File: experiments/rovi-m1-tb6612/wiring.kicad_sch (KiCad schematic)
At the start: 0 parts

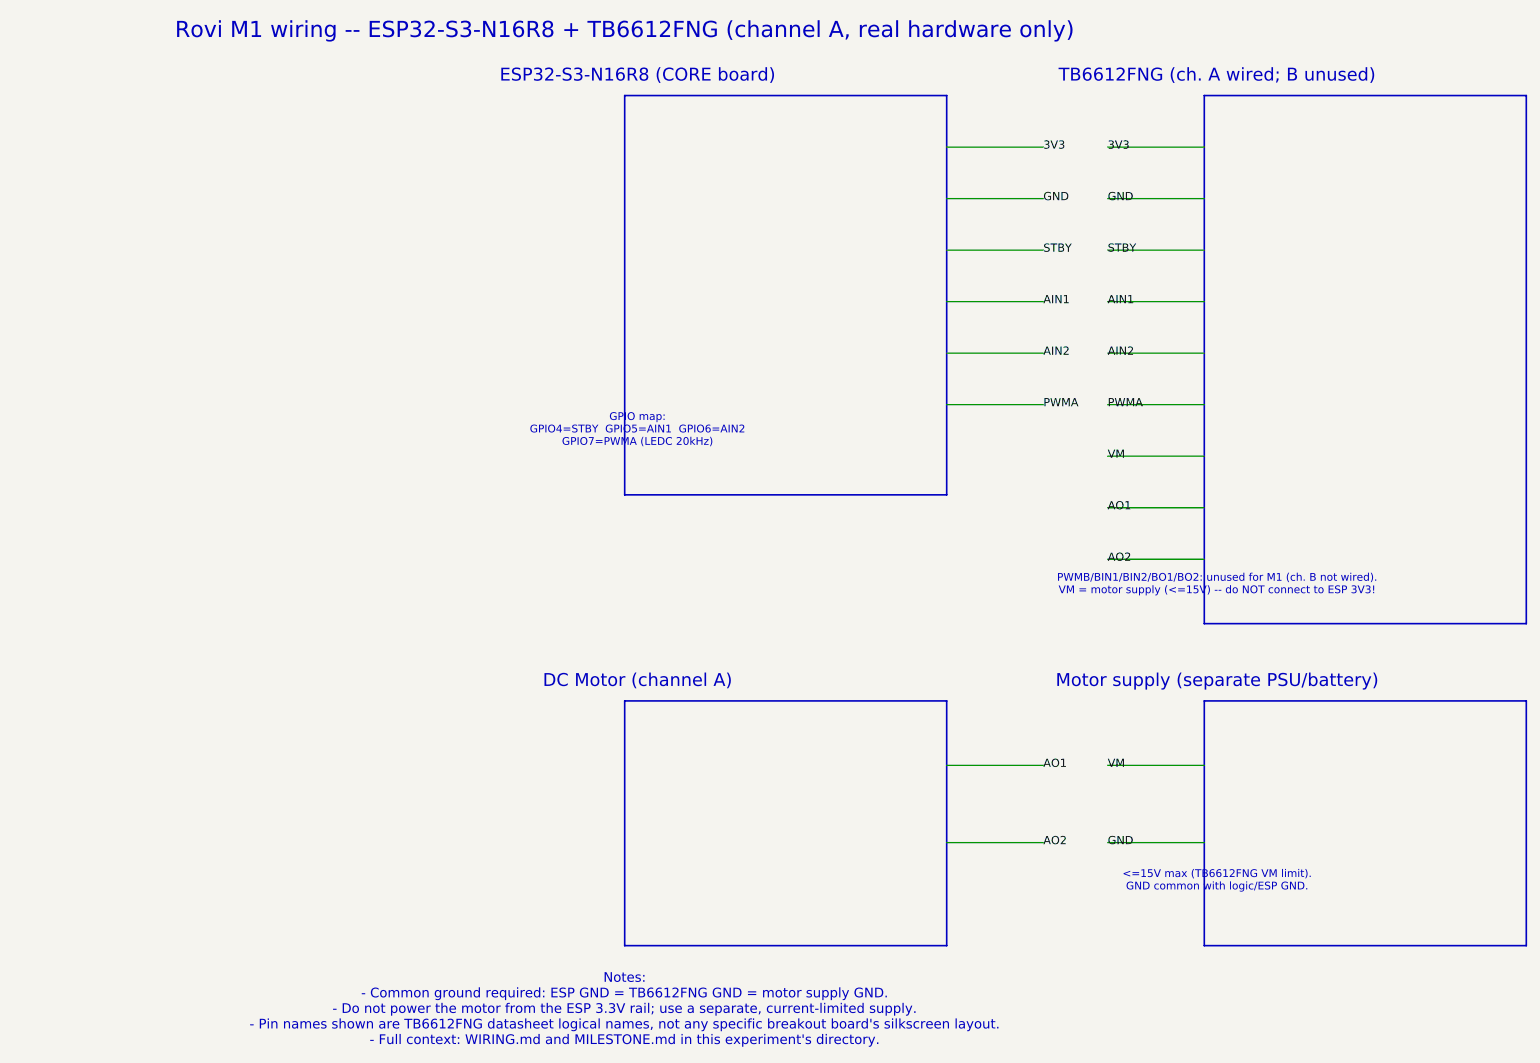
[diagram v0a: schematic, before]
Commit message: Fix wiring.kicad_sch: real component symbols, not floating labels
The previous version drew boxes as plain graphic rectangles and wired
them with net labels that weren't attached to anything electrical --
kicad-cli sch erc correctly flagged all 18 labels as dangling (every
net had no real pin at either end), which is exactly what "incorrect,
missing connections between components" describes.

Rebuilt with four real symbols (ESP32S3, TB6612FNG, MOTOR,
MOTORSUPPLY), each with actual numbered pins and a body rectangle,
placed as proper symbol instances (U1/U2/M1/PS1). Existing wires and
net labels connect directly to the real pin tips now instead of
floating in space. Calibrated the pin angle/Y-axis convention with a
throwaway test file before touching the real one, since getting that
wrong across ~19 pins blind would've meant redoing all of it.

Verified with `kicad-cli sch erc`: 0 errors (was 19), down from 57 to
27 violations, all remaining ones cosmetic (off-grid warnings, and an
expected "library not found" notice since the symbols are embedded
rather than pulled from an installed library). Re-rendered to PDF and
visually confirmed pin numbers/names and net connections read
correctly on every component.

Co-Authored-By: Claude Sonnet 5 <noreply@anthropic.com>
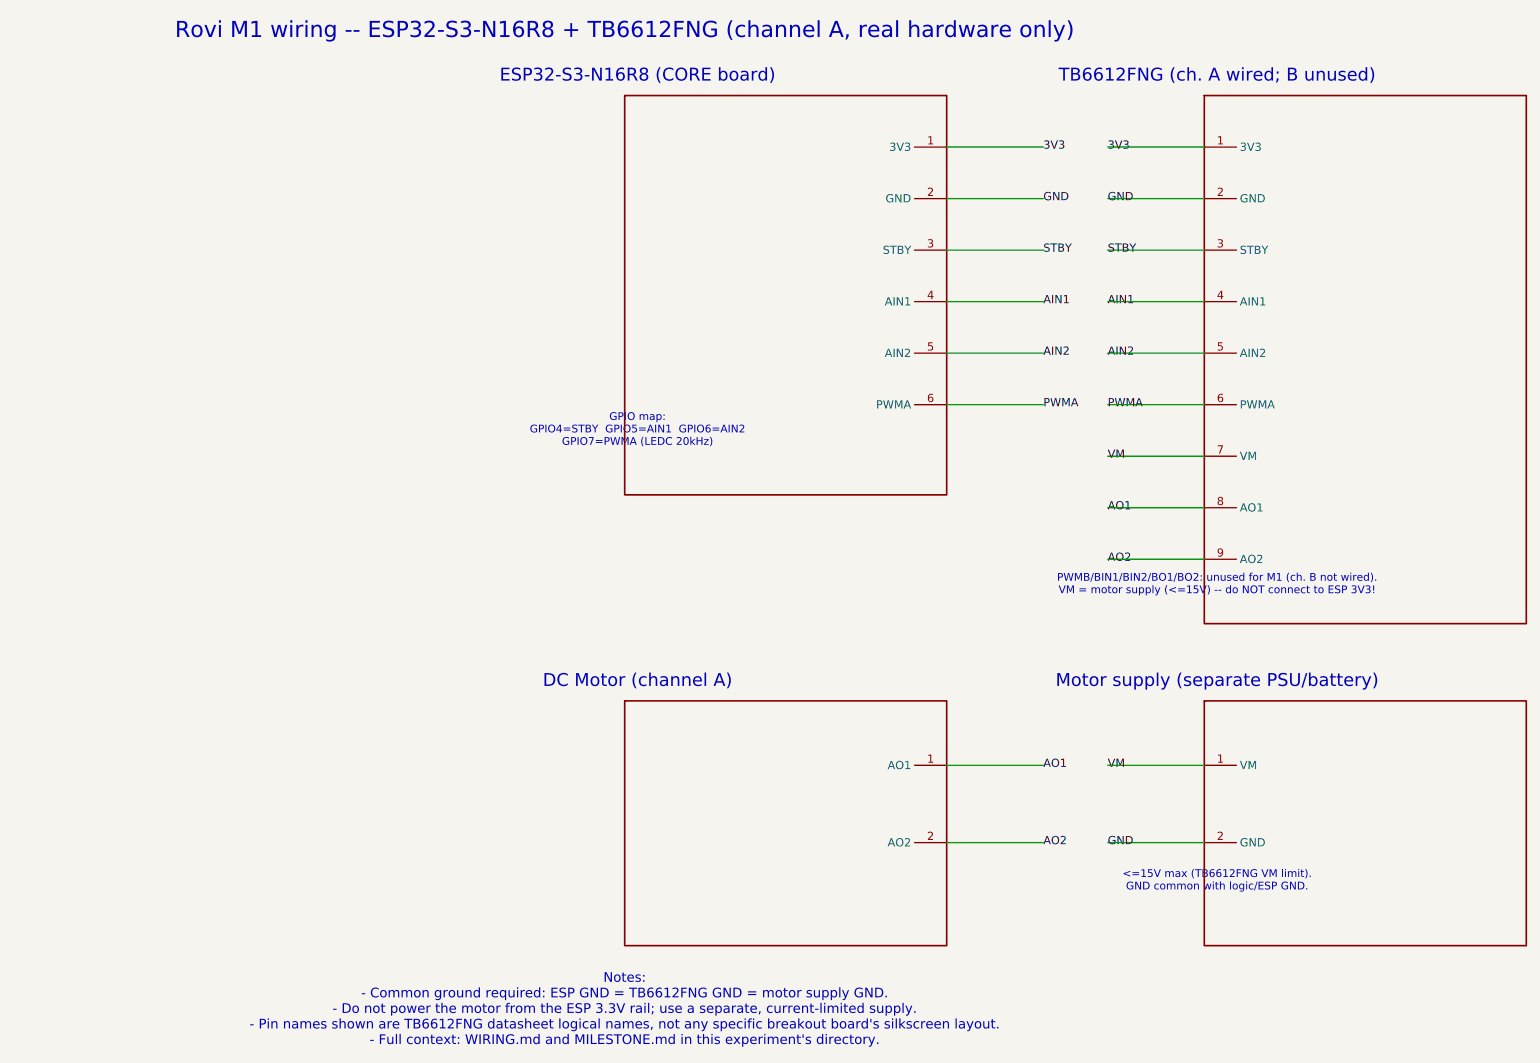
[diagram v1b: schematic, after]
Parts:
- added M1: DC_MOTOR, symbol M1:MOTOR
- added PS1: MOTOR_SUPPLY, symbol M1:MOTORSUPPLY
- added U1: ESP32S3, symbol M1:ESP32S3
- added U2: TB6612FNG, symbol M1:TB6612FNG
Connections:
- net 3V3: now also U1.1 (3V3), U2.1 (3V3)
- net AIN1: now also U1.4 (AIN1), U2.4 (AIN1)
- net AIN2: now also U1.5 (AIN2), U2.5 (AIN2)
- net AO1: now also M1.1 (AO1), U2.8 (AO1)
- net AO2: now also M1.2 (AO2), U2.9 (AO2)
- net GND: now also PS1.2 (GND), U1.2 (GND), U2.2 (GND)
- net PWMA: now also U1.6 (PWMA), U2.6 (PWMA)
- net STBY: now also U1.3 (STBY), U2.3 (STBY)
- net VM: now also PS1.1 (VM), U2.7 (VM)
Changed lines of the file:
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@@
 		(effects (font (size 2.5 2.5)))
 	)
-	(rectangle
-		(start 20 18) (end 70 80)
-		(stroke (width 0.254) (type default))
-		(fill (type none))
+	(symbol (lib_id "M1:ESP32S3") (at 70 26 0) (unit 1) (in_bom yes) (on_board yes)
+		(property "Reference" "U1" (at 20 20 0) (effects (font (size 1.27 1.27)) hide))
+		(property "Value" "ESP32S3" (at 20 25 0) (effects (font (size 1.27 1.27)) hide))
+		(pin "1")
+		(pin "2")
+		(pin "3")
+		(pin "4")
+		(pin "5")
+		(pin "6")
 	)
 	(text "ESP32-S3-N16R8 (CORE board)"
@@
 		(effects (font (size 1.2 1.2)))
 	)
-	(rectangle
-		(start 110 18) (end 160 100)
-		(stroke (width 0.254) (type default))
-		(fill (type none))
+	(symbol (lib_id "M1:TB6612FNG") (at 110 26 0) (unit 1) (in_bom yes) (on_board yes)
+		(property "Reference" "U2" (at 130 20 0) (effects (font (size 1.27 1.27)) hide))
+		(property "Value" "TB6612FNG" (at 130 25 0) (effects (font (size 1.27 1.27)) hide))
+		(pin "1")
+		(pin "2")
+		(pin "3")
+		(pin "4")
+		(pin "5")
+		(pin "6")
+		(pin "7")
+		(pin "8")
+		(pin "9")
 	)
 	(text "TB6612FNG (ch. A wired; B unused)"
@@
 		(effects (font (size 1.2 1.2)))
 	)
-	(rectangle
-		(start 20 112) (end 70 150)
-		(stroke (width 0.254) (type default))
-		(fill (type none))
+	(symbol (lib_id "M1:MOTOR") (at 70 122 0) (unit 1) (in_bom yes) (on_board yes)
+		(property "Reference" "M1" (at 20 132 0) (effects (font (size 1.27 1.27)) hide))
+		(property "Value" "DC_MOTOR" (at 20 137 0) (effects (font (size 1.27 1.27)) hide))
+		(pin "1")
+		(pin "2")
 	)
 	(text "DC Motor (channel A)"
@@
 	(wire (pts (xy 70 134) (xy 85 134)) (stroke (width 0) (type default)))
 	(label "AO2" (at 85 134 0) (effects (font (size 1.27 1.27))))
-	(rectangle
-		(start 110 112) (end 160 150)
-		(stroke (width 0.254) (type default))
-		(fill (type none))
+	(symbol (lib_id "M1:MOTORSUPPLY") (at 110 122 0) (unit 1) (in_bom yes) (on_board yes)
+		(property "Reference" "PS1" (at 130 132 0) (effects (font (size 1.27 1.27)) hide))
+		(property "Value" "MOTOR_SUPPLY" (at 130 137 0) (effects (font (size 1.27 1.27)) hide))
+		(pin "1")
+		(pin "2")
 	)
 	(text "Motor supply (separate PSU/battery)"
